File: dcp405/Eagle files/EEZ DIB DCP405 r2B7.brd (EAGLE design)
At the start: 180 x 95 mm, 322 parts, among them IC1 LTC3864EMSE#PBF, IC10 MC33272ADR2G, IC11 LTC2050HVCS8#PBF, IC12 74AUP1G74DC.125, IC13 MCP23S17-E/SS, IC14 REF5025AIDR, IC15 TC77-5.0MCTTR, IC16 DAC8552IDGKR, IC17 SN74LVC1G3157DCKR, IC18 ADS1120IPWR, IC19 LM293D, IC2 TPS54060DGQ, IC20 MAX9141ESA, IC3 SI8641BB-B-IS1, IC4 SN74LVC1G139DCUR, IC5 MC78L05, IC6 MC79L05, IC7 SI8641BB-B-IS1, IC8 M24C32-WMN6P, IC9 TL072D, J1 4907, J2 FCR7350R, J3 FCR7350B, K1 G6K-2F-5DC, Q1 SUD19P06-60, Q10 PSMN0R9-25YLC, Q11 PSMN0R9-25YLC, Q12 BSS84P, Q13 BTA26-600, Q14 FMMT493TA, Q15 2N7002, Q16 2N7002, Q17 2N7002, Q18 PSMN013-60YL, Q19 MMBT5551, Q2 MMBT5401, Q20 MMBT5401, Q21 MMBT5551, Q22 MMBT5551, Q23 2N7002, Q3 D45H11FP, Q4 D45H11FP, Q5 FQPF11P06 or FQPF27P06, Q6 BCP56-16.115, Q7 MMBT5401, Q8 NZT605, Q9 BSS205NH6327XTSA1, X1 39-30-1020, X2 77317-104-28LF, X3 691322110005, X4 DS1024-2*10R0

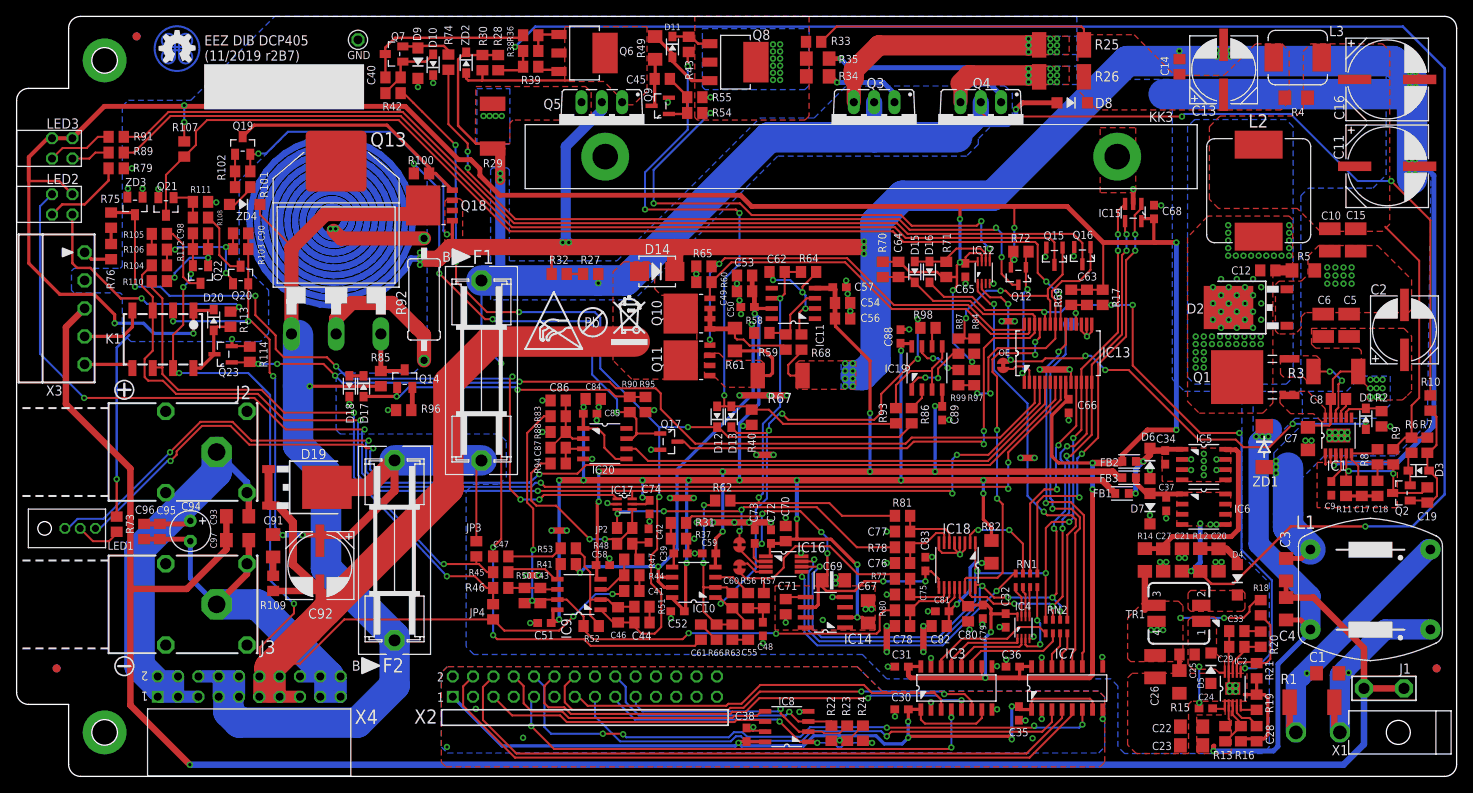
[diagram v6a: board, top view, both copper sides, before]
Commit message: DCP405 R4, R49 package changed
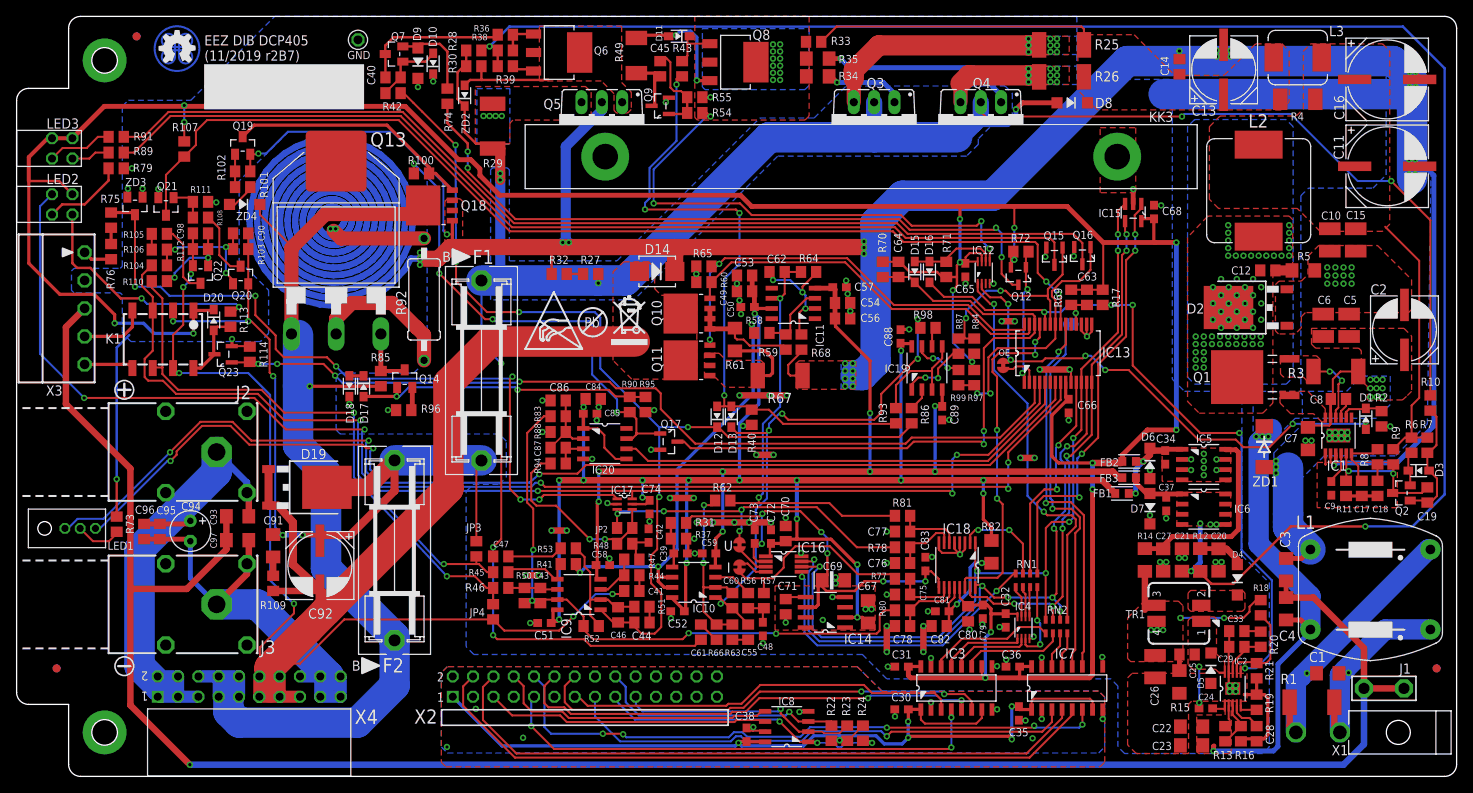
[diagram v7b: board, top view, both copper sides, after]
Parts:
- R4, R49: device rcl:R1206 -> rcl:R2010
- moved R74 4.26 mm to (53.8, 85.0)
- moved ZD2 4.13 mm to (56.0, 85.1), turned to 90 degrees
- moved R28 3.41 mm to (57.1, 90.7), turned to 180 degrees
- moved Q6 3.18 mm to (67.8, 90.5)
- moved R36 3.18 mm to (61.1, 92.7)
- moved R38 3.18 mm to (61.1, 90.7)
- moved R39 3.18 mm to (61.1, 88.8)
- moved R43 3.16 mm to (83.2, 88.5)
- moved R49 2.54 mm to (77.5, 90.1)
- moved D11 1.57 mm to (82.8, 92.5), turned to 180 degrees
- moved C45 1.30 mm to (80.5, 88.5), turned to 270 degrees
- moved R30 1.17 mm to (57.1, 88.8), turned to 0 degrees
- moved R4 0.27 mm to (160.1, 84.6)
- moved D10 0.13 mm to (52.1, 89.1)
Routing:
- net N$47: track 9.67 -> 16.5 mm, vias 0 -> 2
- net N$53: track 7.72 -> 12.5 mm
- net !DP_DRIVE: track 6.63 -> 11.4 mm
- net N$42: track 92.0 -> 87.4 mm
- net POST_OUT+: track 288.7 -> 284.8 mm
- net LOOP_CTRL: track 82.2 -> 79.0 mm
- net Q6C: track 15.5 -> 12.5 mm
- net N$45: track 21.9 -> 18.9 mm
- net -9V: track 223.9 -> 225.6 mm
- net N$46: track 5.04 -> 6.70 mm
- net N$35: track 6.20 -> 7.83 mm
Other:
- board text added: "I"
- board text added: "U"

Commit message: #60
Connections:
- net OUTF+: no longer Q13.A1, Q18.MB, R85.2, ZD4.C
- net POST_OUTF+: now also Q13.A1, Q18.MB, R85.2, ZD4.C
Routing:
- net OUTF+: track 134.8 -> 44.0 mm, vias 1 -> 0
- net POST_OUTF+: track 104.0 -> 154.6 mm, vias 5 -> 3
- net GND: track 202.2 -> 212.2 mm, vias 122 -> 127
- net OE_GREEN: track 137.0 -> 146.2 mm, vias 3 -> 5
- net OE_RED: track 146.1 -> 152.4 mm, vias 5 -> 7
- net POST_OUT-: track 231.2 -> 227.2 mm
- net SENSE-: track 73.6 -> 69.6 mm
- net AUX_USET_SW: track 167.2 -> 163.6 mm
- net SENSE+: track 74.8 -> 71.6 mm
- net +5V: track 400.8 -> 398.5 mm
- net AUX_IN: track 96.1 -> 93.8 mm
- net U_SET_OUT: track 24.4 -> 25.6 mm
- net RSENSE: vias 4 -> 2
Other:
- board text added: "EEZ DIB DCP405 (12/2019 r2B7)"
- board text added: "EEZ DIB DCP405 (12/2019 r2B7) DC power source 0-40V / 5A Project source code: github.com/eez-open"
- board text removed: "EEZ DIB DCP405 (11/2019 r2B7)"
- board text removed: "EEZ DIB DCP405 (11/2019 r2B7) DC power source 0-40V / 5A Project source code: github.com/eez-open"
